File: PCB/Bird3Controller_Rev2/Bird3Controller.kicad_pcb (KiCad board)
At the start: 2 copper layers, 43 x 108 mm, 51 parts, among them J1 Bird 3 24-pin Connector, J2 TXW154028S0 Connector, J3 87832-2220, Q1 2N7002A, SW1 SW_Boot, SW2 SW_Reset, U1 ESP32-S3-WROOM-1, U3 SN65HVD231, U4 LMR36520ADDAR, U5 LM3519MK-20_NOPB

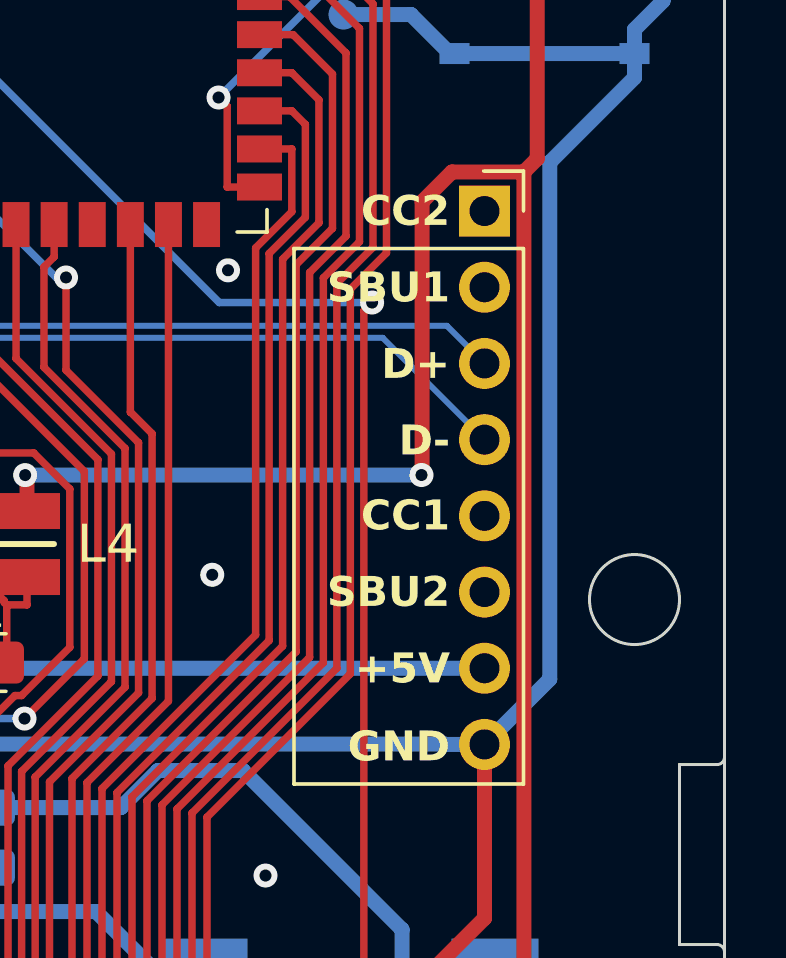
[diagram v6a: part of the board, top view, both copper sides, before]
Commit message: Upgrade Rev2 project and files to KiCad 8 using KiCad 8.0.1
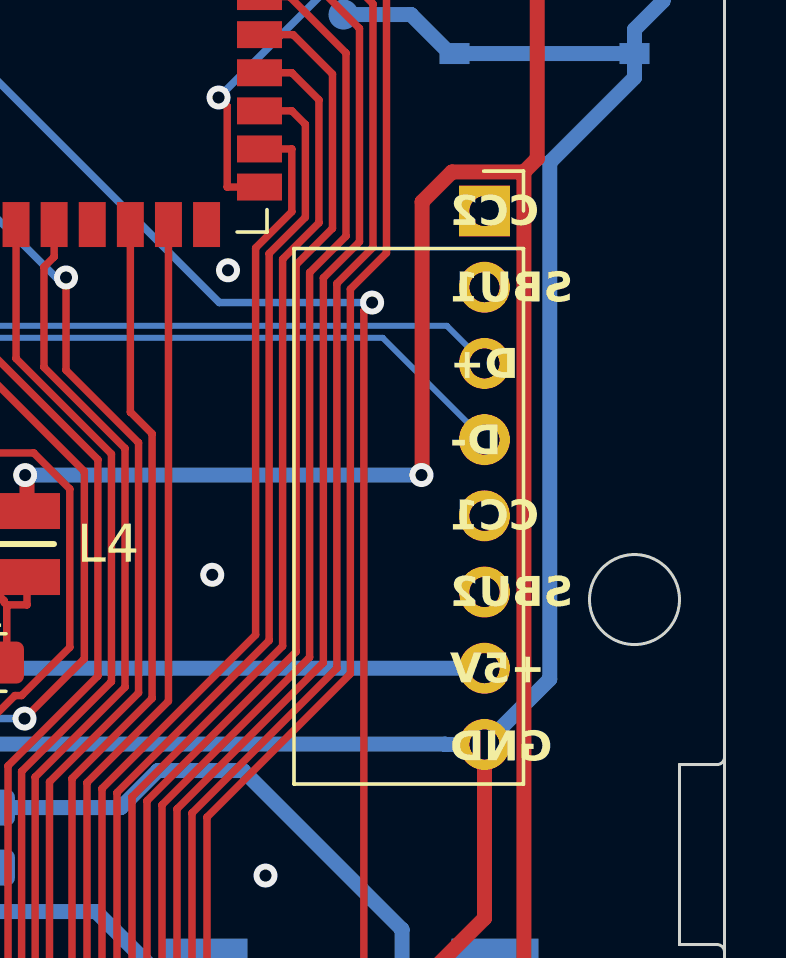
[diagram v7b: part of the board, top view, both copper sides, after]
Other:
- board text added: "Sim Tray Padding"
- board text removed: "locked"
